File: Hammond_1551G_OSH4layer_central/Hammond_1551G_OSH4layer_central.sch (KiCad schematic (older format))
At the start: 4 parts

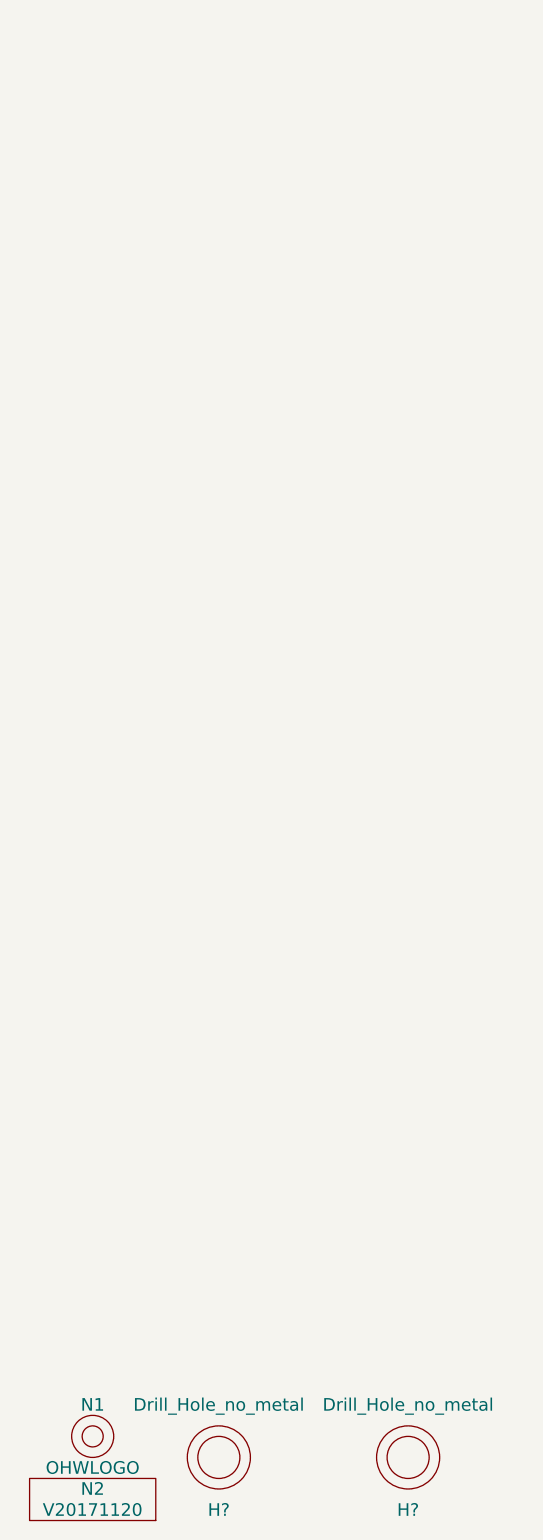
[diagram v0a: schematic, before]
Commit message: DONE: Hammond 1551G, 4 layer, connectored microcontroller template
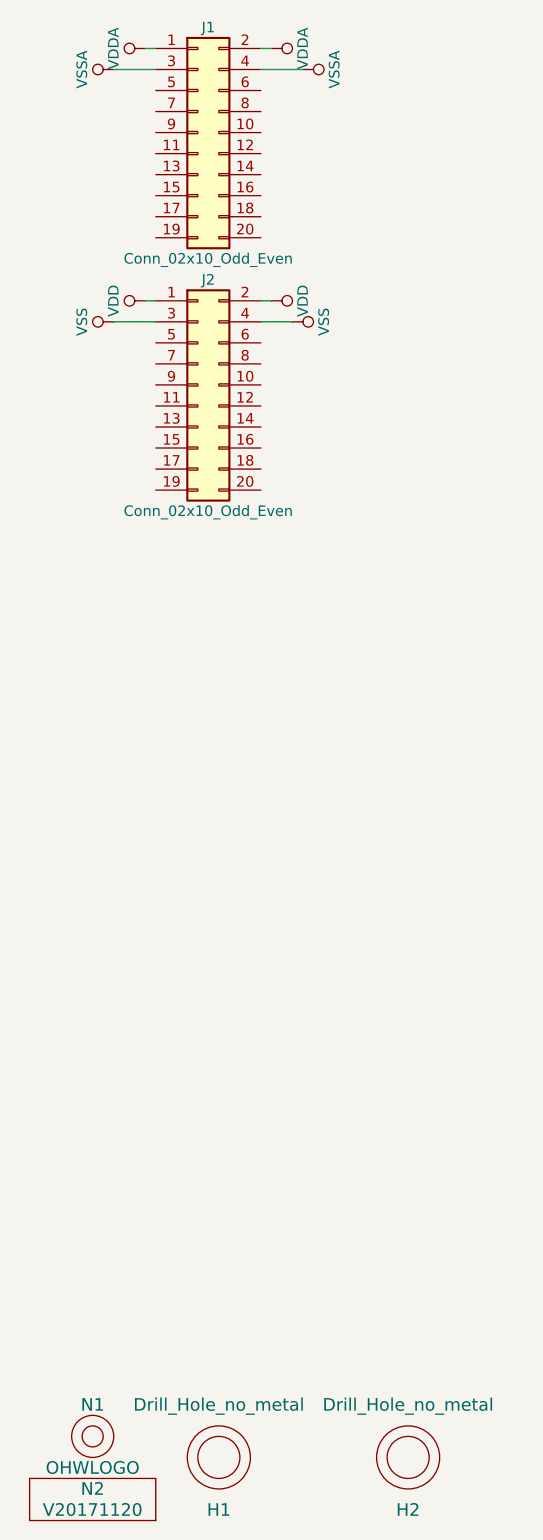
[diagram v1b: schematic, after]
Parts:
- added J1, J2: Conn_02x10_Odd_Even, SquantorConnectors:Header_0127_2X10_H007, symbol Conn_02x10_Odd_Even
- gave numbers to parts that had none: 2
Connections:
- new net VDD: J2.1 (Pin_1), J2.2 (Pin_2)
- new net VDDA: J1.1 (Pin_1), J1.2 (Pin_2)
- new net VSS: J2.3 (Pin_3), J2.4 (Pin_4)
- new net VSSA: J1.3 (Pin_3), J1.4 (Pin_4)
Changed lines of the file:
@@
 LIBS:SquantorPCBOutline
 LIBS:SquantorProto
-LIBS:Hammond_1551G_OSH2layer-cache
+LIBS:Hammond_1551G_OSH4layer_central-cache
 EELAYER 25 0
 EELAYER END
@@
 $EndComp
 $Comp
-L Drill_Hole_no_metal H?
+L Drill_Hole_no_metal H1
 U 1 1 5B1CFFB9
 P 1450 7450
-F 0 "H?" H 1450 7200 60  0000 C CNN
+F 0 "H1" H 1450 7200 60  0000 C CNN
 F 1 "Drill_Hole_no_metal" H 1450 7700 60  0000 C CNN
 F 2 "SquantorPcbOutline:MountingHole_2.5mm_no_metal" H 1450 7450 60  0001 C CNN
@@
 $EndComp
 $Comp
-L Drill_Hole_no_metal H?
+L Drill_Hole_no_metal H2
 U 1 1 5B1D000C
 P 2350 7450
-F 0 "H?" H 2350 7200 60  0000 C CNN
+F 0 "H2" H 2350 7200 60  0000 C CNN
 F 1 "Drill_Hole_no_metal" H 2350 7700 60  0000 C CNN
 F 2 "SquantorPcbOutline:MountingHole_2.5mm_no_metal" H 2350 7450 60  0001 C CNN
@@
 	1    0    0    -1
 $EndComp
+$Comp
+L Conn_02x10_Odd_Even J1
+U 1 1 5B1D0821
+P 1350 1150
+F 0 "J1" H 1400 1650 50  0000 C CNN
+F 1 "Conn_02x10_Odd_Even" H 1400 550 50  0000 C CNN
+F 2 "SquantorConnectors:Header_0127_2X10_H007" H 1350 1150 50  0001 C CNN
+F 3 "" H 1350 1150 50  0001 C CNN
+	1    1350 1150
+	1    0    0    -1
+$EndComp
+$Comp
+L VSSA #PWR01
+U 1 1 5B1D0A66
+P 1850 850
+F 0 "#PWR01" H 1850 700 50  0001 C CNN
+F 1 "VSSA" H 1850 1000 50  0000 C CNN
+F 2 "" H 1850 850 50  0001 C CNN
+F 3 "" H 1850 850 50  0001 C CNN
+	1    1850 850
+	0    1    1    0
+$EndComp
+$Comp
+L VSSA #PWR02
+U 1 1 5B1D0A8A
+P 950 850
+F 0 "#PWR02" H 950 700 50  0001 C CNN
+F 1 "VSSA" H 950 1000 50  0000 C CNN
+F 2 "" H 950 850 50  0001 C CNN
+F 3 "" H 950 850 50  0001 C CNN
+	1    950  850
+	0    -1   -1   0
+$EndComp
+$Comp
+L VDDA #PWR03
+U 1 1 5B1D0AA3
+P 1700 750
+F 0 "#PWR03" H 1700 600 50  0001 C CNN
+F 1 "VDDA" H 1700 900 50  0000 C CNN
+F 2 "" H 1700 750 50  0001 C CNN
+F 3 "" H 1700 750 50  0001 C CNN
+	1    1700 750
+	0    1    1    0
+$EndComp
+$Comp
+L VDDA #PWR04
+U 1 1 5B1D0AC7
+P 1100 750
+F 0 "#PWR04" H 1100 600 50  0001 C CNN
+F 1 "VDDA" H 1100 900 50  0000 C CNN
+F 2 "" H 1100 750 50  0001 C CNN
+F 3 "" H 1100 750 50  0001 C CNN
+	1    1100 750
+	0    -1   -1   0
+$EndComp
+Wire Wire Line
+	1100 750  1150 750
+Wire Wire Line
+	1150 850  950  850
+Wire Wire Line
+	1650 750  1700 750
+Wire Wire Line
+	1650 850  1850 850
+$Comp
+L VDD #PWR05
+U 1 1 5B1D0E6A
+P 1700 1950
+F 0 "#PWR05" H 1700 1800 50  0001 C CNN
+F 1 "VDD" H 1700 2100 50  0000 C CNN
+F 2 "" H 1700 1950 50  0001 C CNN
+F 3 "" H 1700 1950 50  0001 C CNN
+	1    1700 1950
+	0    1    1    0
+$EndComp
+$Comp
+L VDD #PWR06
+U 1 1 5B1D0E8E
+P 1100 1950
+F 0 "#PWR06" H 1100 1800 50  0001 C CNN
+F 1 "VDD" H 1100 2100 50  0000 C CNN
+F 2 "" H 1100 1950 50  0001 C CNN
+F 3 "" H 1100 1950 50  0001 C CNN
+	1    1100 1950
+	0    -1   -1   0
+$EndComp
+Wire Wire Line
+	1650 1950 1700 1950
+Wire Wire Line
+	1150 1950 1100 1950
+Wire Wire Line
+	1800 2050 1650 2050
+Wire Wire Line
+	1150 2050 950  2050
+$Comp
+L VSS #PWR07
+U 1 1 5B1D15B4
+P 1800 2050
+F 0 "#PWR07" H 1800 1900 50  0001 C CNN
+F 1 "VSS" H 1800 2200 50  0000 C CNN
+F 2 "" H 1800 2050 50  0001 C CNN
+F 3 "" H 1800 2050 50  0001 C CNN
+	1    1800 2050
+	0    1    1    0
+$EndComp
+$Comp
+L VSS #PWR08
+U 1 1 5B1D15EA
+P 950 2050
+F 0 "#PWR08" H 950 1900 50  0001 C CNN
+F 1 "VSS" H 950 2200 50  0000 C CNN
+F 2 "" H 950 2050 50  0001 C CNN
+F 3 "" H 950 2050 50  0001 C CNN
+	1    950  2050
+	0    -1   -1   0
+$EndComp
+$Comp
+L Conn_02x10_Odd_Even J2
+U 1 1 5B1D18B3
+P 1350 2350
+F 0 "J2" H 1400 2850 50  0000 C CNN
+F 1 "Conn_02x10_Odd_Even" H 1400 1750 50  0000 C CNN
+F 2 "SquantorConnectors:Header_0127_2X10_H007" H 1350 2350 50  0001 C CNN
+F 3 "" H 1350 2350 50  0001 C CNN
+	1    1350 2350
+	1    0    0    -1
+$EndComp

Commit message: DONE: added some net names
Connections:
- net ANALOG_05: now reaches J1.10 (Pin_10)
- net ANALOG_06: now reaches J1.11 (Pin_11)
- net ANALOG_07: now reaches J1.12 (Pin_12)
- net ANALOG_08: now reaches J1.13 (Pin_13)
- net ANALOG_09: now reaches J1.14 (Pin_14)
- net ANALOG_10: now reaches J1.15 (Pin_15)
- net ANALOG_11: now reaches J1.16 (Pin_16)
- net ANALOG_12: now reaches J1.17 (Pin_17)
- net ANALOG_13: now reaches J1.18 (Pin_18)
- net ANALOG_14: now reaches J1.19 (Pin_19)
- net ANALOG_15: now reaches J1.20 (Pin_20)
- net ANALOG_00: now reaches J1.5 (Pin_5)
- net ANALOG_01: now reaches J1.6 (Pin_6)
- net ANALOG_02: now reaches J1.7 (Pin_7)
- net ANALOG_03: now reaches J1.8 (Pin_8)
- net ANALOG_04: now reaches J1.9 (Pin_9)
- net DIGITAL_05: now reaches J2.10 (Pin_10)
- net DIGITAL_06: now reaches J2.11 (Pin_11)
- net DIGITAL_07: now reaches J2.12 (Pin_12)
- net DIGITAL_08: now reaches J2.13 (Pin_13)
- net DIGITAL_09: now reaches J2.14 (Pin_14)
- net DIGITAL_10: now reaches J2.15 (Pin_15)
- net DIGITAL_11: now reaches J2.16 (Pin_16)
- net DIGITAL_12: now reaches J2.17 (Pin_17)
- net DIGITAL_13: now reaches J2.18 (Pin_18)
- net DIGITAL_14: now reaches J2.19 (Pin_19)
- net DIGITAL_15: now reaches J2.20 (Pin_20)
- net DIGITAL_00: now reaches J2.5 (Pin_5)
- net DIGITAL_01: now reaches J2.6 (Pin_6)
- net DIGITAL_02: now reaches J2.7 (Pin_7)
- net DIGITAL_03: now reaches J2.8 (Pin_8)
- net DIGITAL_04: now reaches J2.9 (Pin_9)
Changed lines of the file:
@@
 LIBS:SquantorPCBOutline
 LIBS:SquantorProto
-LIBS:Hammond_1551G_OSH4layer_central-cache
+LIBS:nickel_beetle_breakout-cache
 EELAYER 25 0
 EELAYER END
@@
 	1    0    0    -1
 $EndComp
+Wire Wire Line
+	1150 950  1100 950
+Text Label 1100 950  2    60   ~ 0
+ANALOG_00
+Wire Wire Line
+	1150 1050 1100 1050
+Wire Wire Line
+	1150 1150 1100 1150
+Wire Wire Line
+	1150 1250 1100 1250
+Wire Wire Line
+	1150 1350 1100 1350
+Wire Wire Line
+	1150 1450 1100 1450
+Wire Wire Line
+	1150 1550 1100 1550
+Wire Wire Line
+	1150 1650 1100 1650
+Wire Wire Line
+	1650 950  1700 950
+Wire Wire Line
+	1650 1050 1700 1050
+Wire Wire Line
+	1650 1150 1700 1150
+Wire Wire Line
+	1650 1250 1700 1250
+Wire Wire Line
+	1650 1350 1700 1350
+Wire Wire Line
+	1650 1450 1700 1450
+Wire Wire Line
+	1650 1550 1700 1550
+Wire Wire Line
+	1650 1650 1700 1650
+Text Label 1100 1050 2    60   ~ 0
+ANALOG_02
+Text Label 1100 1150 2    60   ~ 0
+ANALOG_04
+Text Label 1100 1250 2    60   ~ 0
+ANALOG_06
+Text Label 1100 1350 2    60   ~ 0
+ANALOG_08
+Text Label 1100 1450 2    60   ~ 0
+ANALOG_10
+Text Label 1100 1550 2    60   ~ 0
+ANALOG_12
+Text Label 1100 1650 2    60   ~ 0
+ANALOG_14
+Text Label 1700 950  0    60   ~ 0
+ANALOG_01
+Text Label 1700 1050 0    60   ~ 0
+ANALOG_03
+Text Label 1700 1150 0    60   ~ 0
+ANALOG_05
+Text Label 1700 1250 0    60   ~ 0
+ANALOG_07
+Text Label 1700 1350 0    60   ~ 0
+ANALOG_09
+Text Label 1700 1450 0    60   ~ 0
+ANALOG_11
+Text Label 1700 1550 0    60   ~ 0
+ANALOG_13
+Text Label 1700 1650 0    60   ~ 0
+ANALOG_15
+Wire Wire Line
+	1150 2150 1100 2150
+Wire Wire Line
+	1150 2250 1100 2250
+Wire Wire Line
+	1150 2350 1100 2350
+Wire Wire Line
+	1150 2450 1100 2450
+Wire Wire Line
+	1150 2550 1100 2550
+Wire Wire Line
+	1150 2650 1100 2650
+Wire Wire Line
+	1150 2750 1100 2750
+Wire Wire Line
+	1150 2850 1100 2850
+Wire Wire Line
+	1650 2150 1700 2150
+Wire Wire Line
+	1650 2250 1700 2250
+Wire Wire Line
+	1650 2350 1700 2350
+Wire Wire Line
+	1650 2450 1700 2450
+Wire Wire Line
+	1650 2550 1700 2550
+Wire Wire Line
+	1650 2650 1700 2650
+Wire Wire Line
+	1650 2750 1700 2750
+Wire Wire Line
+	1650 2850 1700 2850
+Text Label 1100 2150 2    60   ~ 0
+DIGITAL_00
+Text Label 1100 2250 2    60   ~ 0
+DIGITAL_02
+Text Label 1100 2350 2    60   ~ 0
+DIGITAL_04
+Text Label 1100 2450 2    60   ~ 0
+DIGITAL_06
+Text Label 1100 2550 2    60   ~ 0
+DIGITAL_08
+Text Label 1100 2650 2    60   ~ 0
+DIGITAL_10
+Text Label 1100 2750 2    60   ~ 0
+DIGITAL_12
+Text Label 1100 2850 2    60   ~ 0
+DIGITAL_14
+Text Label 1700 2150 0    60   ~ 0
+DIGITAL_01
+Text Label 1700 2250 0    60   ~ 0
+DIGITAL_03
+Text Label 1700 2350 0    60   ~ 0
+DIGITAL_05
+Text Label 1700 2450 0    60   ~ 0
+DIGITAL_07
+Text Label 1700 2550 0    60   ~ 0
+DIGITAL_09
+Text Label 1700 2650 0    60   ~ 0
+DIGITAL_11
+Text Label 1700 2750 0    60   ~ 0
+DIGITAL_13
+Text Label 1700 2850 0    60   ~ 0
+DIGITAL_15
 $EndSCHEMATC

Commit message: DONE: updated header footprints
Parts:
- J1, J2: footprint SquantorConnectors:Header_0127_2X10_H007 -> SquantorConnectors:Header-0127-2X10-H006
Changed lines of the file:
@@
 LIBS:SquantorPCBOutline
 LIBS:SquantorProto
-LIBS:nickel_beetle_breakout-cache
+LIBS:Hammond_1551G_OSH4layer_central-cache
 EELAYER 25 0
 EELAYER END
@@
 F 0 "J1" H 1400 1650 50  0000 C CNN
 F 1 "Conn_02x10_Odd_Even" H 1400 550 50  0000 C CNN
-F 2 "SquantorConnectors:Header_0127_2X10_H007" H 1350 1150 50  0001 C CNN
+F 2 "SquantorConnectors:Header-0127-2X10-H006" H 1350 1150 50  0001 C CNN
 F 3 "" H 1350 1150 50  0001 C CNN
 	1    1350 1150
@@
 F 0 "J2" H 1400 2850 50  0000 C CNN
 F 1 "Conn_02x10_Odd_Even" H 1400 1750 50  0000 C CNN
-F 2 "SquantorConnectors:Header_0127_2X10_H007" H 1350 2350 50  0001 C CNN
+F 2 "SquantorConnectors:Header-0127-2X10-H006" H 1350 2350 50  0001 C CNN
 F 3 "" H 1350 2350 50  0001 C CNN
 	1    1350 2350

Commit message: updated hammond 4 layer oshpark central template
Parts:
- H1, H2: symbol Drill_Hole_no_metal -> SquantorPCBOutline:Drill_Hole_no_metal
- J1, J2: symbol Conn_02x10_Odd_Even -> Connector_Generic:Conn_02x10_Odd_Even
- N1: symbol OHWLOGO -> SquantorLabels:OHWLOGO
- N2: symbol VYYYYMMDD -> SquantorLabels:VYYYYMMDD
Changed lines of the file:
@@
-EESchema Schematic File Version 2
-LIBS:power
-LIBS:device
-LIBS:switches
-LIBS:relays
-LIBS:motors
-LIBS:transistors
-LIBS:conn
-LIBS:linear
-LIBS:regul
-LIBS:74xx
-LIBS:cmos4000
-LIBS:adc-dac
-LIBS:memory
-LIBS:xilinx
-LIBS:microcontrollers
-LIBS:dsp
-LIBS:microchip
-LIBS:analog_switches
-LIBS:motorola
-LIBS:texas
-LIBS:intel
-LIBS:audio
-LIBS:interface
-LIBS:digital-audio
-LIBS:philips
-LIBS:display
-LIBS:cypress
-LIBS:siliconi
-LIBS:opto
-LIBS:atmel
-LIBS:contrib
-LIBS:valves
-LIBS:SquantorButtons
-LIBS:SquantorConnectors
-LIBS:SquantorLabels
-LIBS:SquantorPCBOutline
-LIBS:SquantorProto
+EESchema Schematic File Version 4
 LIBS:Hammond_1551G_OSH4layer_central-cache
-EELAYER 25 0
+EELAYER 26 0
 EELAYER END
 $Descr A4 11693 8268
@@
 $EndDescr
 $Comp
-L VYYYYMMDD N2
+L SquantorLabels:VYYYYMMDD N2
 U 1 1 5A1357A5
 P 850 7700
@@
 $EndComp
 $Comp
-L OHWLOGO N1
+L SquantorLabels:OHWLOGO N1
 U 1 1 5A135869
 P 850 7350
@@
 $EndComp
 $Comp
-L Drill_Hole_no_metal H1
+L SquantorPCBOutline:Drill_Hole_no_metal H1
 U 1 1 5B1CFFB9
 P 1450 7450
@@
 $EndComp
 $Comp
-L Drill_Hole_no_metal H2
+L SquantorPCBOutline:Drill_Hole_no_metal H2
 U 1 1 5B1D000C
 P 2350 7450
@@
 $EndComp
 $Comp
-L Conn_02x10_Odd_Even J1
+L Connector_Generic:Conn_02x10_Odd_Even J1
 U 1 1 5B1D0821
 P 1350 1150
@@
 $EndComp
 $Comp
-L VSSA #PWR01
+L power:VSSA #PWR01
 U 1 1 5B1D0A66
 P 1850 850
@@
 $EndComp
 $Comp
-L VSSA #PWR02
+L power:VSSA #PWR02
 U 1 1 5B1D0A8A
 P 950 850
@@
 $EndComp
 $Comp
-L VDDA #PWR03
+L power:VDDA #PWR03
 U 1 1 5B1D0AA3
 P 1700 750
@@
 $EndComp
 $Comp
-L VDDA #PWR04
+L power:VDDA #PWR04
 U 1 1 5B1D0AC7
 P 1100 750
@@
 	1650 850  1850 850
 $Comp
-L VDD #PWR05
+L power:VDD #PWR05
 U 1 1 5B1D0E6A
 P 1700 1950
@@
 $EndComp
 $Comp
-L VDD #PWR06
+L power:VDD #PWR06
 U 1 1 5B1D0E8E
 P 1100 1950
@@
 	1150 2050 950  2050
 $Comp
-L VSS #PWR07
+L power:VSS #PWR07
 U 1 1 5B1D15B4
 P 1800 2050
@@
 $EndComp
 $Comp
-L VSS #PWR08
+L power:VSS #PWR08
 U 1 1 5B1D15EA
 P 950 2050
@@
 $EndComp
 $Comp
-L Conn_02x10_Odd_Even J2
+L Connector_Generic:Conn_02x10_Odd_Even J2
 U 1 1 5B1D18B3
 P 1350 2350
